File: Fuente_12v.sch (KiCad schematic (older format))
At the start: 3 parts, among them U1 L7812

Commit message: agregado el segundo RDC, leds conectados a +5v, asignados footprints
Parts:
- removed C1: 10µ, symbol Device:CP
- added C1: 10µ, Capacitor_SMD:CP_Elec_4x5.4, symbol Device:CP1
- C2: footprint (none) -> Capacitor_SMD:C_1206_3216Metric_Pad1.42x1.75mm_HandSolder
- U1: footprint (none) -> Package_TO_SOT_THT:TO-218-3_Vertical
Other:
- note added: "Ver la corriente que consumen los RDC \npara no superar 1A que suministra el LM7812"
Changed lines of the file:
@@
 $Descr A4 11693 8268
 encoding utf-8
-Sheet 2 4
+Sheet 5 5
 Title ""
 Date ""
@@
 F 0 "U1" H 3100 2342 50  0000 C CNN
 F 1 "L7812" H 3100 2251 50  0000 C CNN
-F 2 "" H 3125 1950 50  0001 L CIN
+F 2 "Package_TO_SOT_THT:TO-218-3_Vertical" H 3125 1950 50  0001 L CIN
 F 3 "http://www.st.com/content/ccc/resource/technical/document/datasheet/41/4f/b3/b0/12/d4/47/88/CD00000444.pdf/files/CD00000444.pdf/jcr:content/translations/en.CD00000444.pdf" H 3100 2050 50  0001 C CNN
 	1    3100 2100
 	1    0    0    -1
 $EndComp
-$Comp
-L Device:CP C?
-U 1 1 5EF448FC
-P 3600 2250
-AR Path="/5EF448FC" Ref="C?"  Part="1"
-AR Path="/5EF34214/5EF448FC" Ref="C1"  Part="1"
-F 0 "C1" H 3718 2296 50  0000 L CNN
-F 1 "10µ" H 3718 2205 50  0000 L CNN
-F 2 "" H 3638 2100 50  0001 C CNN
-F 3 "~" H 3600 2250 50  0001 C CNN
-	1    3600 2250
-	1    0    0    -1
-$EndComp
-Wire Wire Line
-	3400 2100 3600 2100
 $Comp
 L power:GND #PWR?
@@
 F 0 "C2" H 4165 2296 50  0000 L CNN
 F 1 "0,1µ" H 4165 2205 50  0000 L CNN
-F 2 "" H 4088 2100 50  0001 C CNN
+F 2 "Capacitor_SMD:C_1206_3216Metric_Pad1.42x1.75mm_HandSolder" H 4088 2100 50  0001 C CNN
 F 3 "~" H 4050 2250 50  0001 C CNN
 	1    4050 2250
@@
 Wire Wire Line
 	4050 2400 4050 2450
-Wire Wire Line
-	3600 2100 4050 2100
-Connection ~ 3600 2100
 $Comp
 L power:+12V #PWR?
@@
 Wire Wire Line
 	2500 2100 2800 2100
+$Comp
+L Device:CP1 C1
+U 1 1 5F0A8BCC
+P 3600 2250
+F 0 "C1" H 3715 2296 50  0000 L CNN
+F 1 "10µ" H 3715 2205 50  0000 L CNN
+F 2 "Capacitor_SMD:CP_Elec_4x5.4" H 3600 2250 50  0001 C CNN
+F 3 "~" H 3600 2250 50  0001 C CNN
+	1    3600 2250
+	1    0    0    -1
+$EndComp
+Wire Wire Line
+	3400 2100 3600 2100
+Connection ~ 3600 2100
+Wire Wire Line
+	3600 2100 4050 2100
+Text Notes 2350 1800 0    50   ~ 0
+Ver la corriente que consumen los RDC \npara no superar 1A que suministra el LM7812
 $EndSCHEMATC

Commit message: cambios en el placement
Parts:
- renumbered C1 to C26, C2 to C27, U1 to U3
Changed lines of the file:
@@
 P 3100 2100
 AR Path="/5EF448F6" Ref="U?"  Part="1"
-AR Path="/5EF34214/5EF448F6" Ref="U1"  Part="1"
-F 0 "U1" H 3100 2342 50  0000 C CNN
+AR Path="/5EF34214/5EF448F6" Ref="U3"  Part="1"
+F 0 "U3" H 3100 2342 50  0000 C CNN
 F 1 "L7812" H 3100 2251 50  0000 C CNN
 F 2 "Package_TO_SOT_THT:TO-218-3_Vertical" H 3125 1950 50  0001 L CIN
@@
 P 3100 2450
 AR Path="/5EF44904" Ref="#PWR?"  Part="1"
-AR Path="/5EF34214/5EF44904" Ref="#PWR0102"  Part="1"
-F 0 "#PWR0102" H 3100 2450 30  0001 C CNN
+AR Path="/5EF34214/5EF44904" Ref="#PWR046"  Part="1"
+F 0 "#PWR046" H 3100 2450 30  0001 C CNN
 F 1 "GND" H 3100 2380 30  0001 C CNN
 F 2 "" H 3100 2450 60  0000 C CNN
@@
 P 3600 2450
 AR Path="/5EF4490B" Ref="#PWR?"  Part="1"
-AR Path="/5EF34214/5EF4490B" Ref="#PWR0103"  Part="1"
-F 0 "#PWR0103" H 3600 2450 30  0001 C CNN
+AR Path="/5EF34214/5EF4490B" Ref="#PWR047"  Part="1"
+F 0 "#PWR047" H 3600 2450 30  0001 C CNN
 F 1 "GND" H 3600 2380 30  0001 C CNN
 F 2 "" H 3600 2450 60  0000 C CNN
@@
 P 4050 2250
 AR Path="/5EF44912" Ref="C?"  Part="1"
-AR Path="/5EF34214/5EF44912" Ref="C2"  Part="1"
-F 0 "C2" H 4165 2296 50  0000 L CNN
+AR Path="/5EF34214/5EF44912" Ref="C27"  Part="1"
+F 0 "C27" H 4165 2296 50  0000 L CNN
 F 1 "0,1µ" H 4165 2205 50  0000 L CNN
 F 2 "Capacitor_SMD:C_1206_3216Metric_Pad1.42x1.75mm_HandSolder" H 4088 2100 50  0001 C CNN
@@
 P 4050 2450
 AR Path="/5EF44918" Ref="#PWR?"  Part="1"
-AR Path="/5EF34214/5EF44918" Ref="#PWR0104"  Part="1"
-F 0 "#PWR0104" H 4050 2450 30  0001 C CNN
+AR Path="/5EF34214/5EF44918" Ref="#PWR048"  Part="1"
+F 0 "#PWR048" H 4050 2450 30  0001 C CNN
 F 1 "GND" H 4050 2380 30  0001 C CNN
 F 2 "" H 4050 2450 60  0000 C CNN
@@
 P 4500 2100
 AR Path="/5EF44921" Ref="#PWR?"  Part="1"
-AR Path="/5EF34214/5EF44921" Ref="#PWR0105"  Part="1"
-F 0 "#PWR0105" H 4500 1950 50  0001 C CNN
+AR Path="/5EF34214/5EF44921" Ref="#PWR045"  Part="1"
+F 0 "#PWR045" H 4500 1950 50  0001 C CNN
 F 1 "+12V" H 4515 2273 50  0000 C CNN
 F 2 "" H 4500 2100 50  0001 C CNN
@@
 P 2500 2100
 AR Path="/5EF448F0" Ref="#PWR?"  Part="1"
-AR Path="/5EF34214/5EF448F0" Ref="#PWR0101"  Part="1"
-F 0 "#PWR0101" H 2500 1950 50  0001 C CNN
+AR Path="/5EF34214/5EF448F0" Ref="#PWR044"  Part="1"
+F 0 "#PWR044" H 2500 1950 50  0001 C CNN
 F 1 "+24V" H 2515 2273 50  0000 C CNN
 F 2 "" H 2500 2100 50  0001 C CNN
@@
 	2500 2100 2800 2100
 $Comp
-L Device:CP1 C1
+L Device:CP1 C26
 U 1 1 5F0A8BCC
 P 3600 2250
-F 0 "C1" H 3715 2296 50  0000 L CNN
+F 0 "C26" H 3715 2296 50  0000 L CNN
 F 1 "10µ" H 3715 2205 50  0000 L CNN
 F 2 "Capacitor_SMD:CP_Elec_4x5.4" H 3600 2250 50  0001 C CNN

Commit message: reubicados componentes, cambiado regulador a SMD
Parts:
- U3: footprint Package_TO_SOT_THT:TO-218-3_Vertical -> Package_TO_SOT_SMD:TO-252-3_TabPin2
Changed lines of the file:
@@
 F 0 "U3" H 3100 2342 50  0000 C CNN
 F 1 "L7812" H 3100 2251 50  0000 C CNN
-F 2 "Package_TO_SOT_THT:TO-218-3_Vertical" H 3125 1950 50  0001 L CIN
+F 2 "Package_TO_SOT_SMD:TO-252-3_TabPin2" H 3125 1950 50  0001 L CIN
 F 3 "http://www.st.com/content/ccc/resource/technical/document/datasheet/41/4f/b3/b0/12/d4/47/88/CD00000444.pdf/files/CD00000444.pdf/jcr:content/translations/en.CD00000444.pdf" H 3100 2050 50  0001 C CNN
 	1    3100 2100

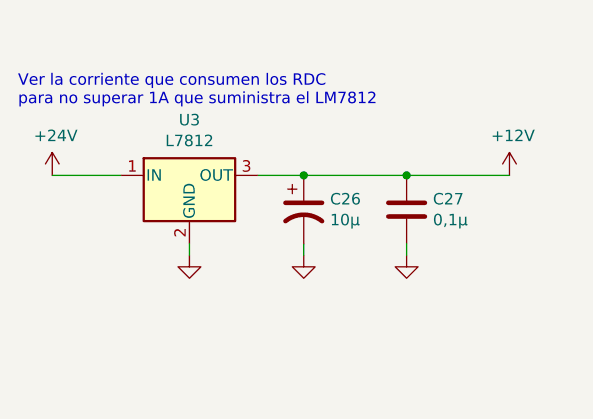
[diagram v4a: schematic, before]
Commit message: cambiado a conectores MOLEX KK, agregados test points para señales analogicas
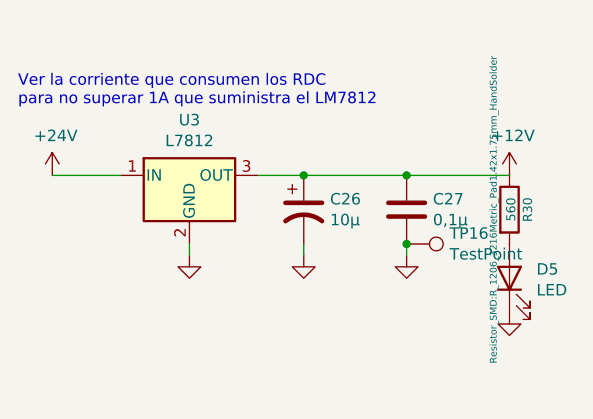
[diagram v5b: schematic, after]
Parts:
- added D5: LED, LED_SMD:LED_1206_3216Metric_Pad1.42x1.75mm_HandSolder, symbol Device:LED
- added R30: 560, Resistor_SMD:R_1206_3216Metric_Pad1.42x1.75mm_HandSolder, symbol Device:R
- added TP16: TestPoint, TestPoint:TestPoint_THTPad_1.0x1.0mm_Drill0.5mm, symbol Connector:TestPoint
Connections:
- net +12V: now also R30.1
- net GND: now also D5.1 (K), TP16.1
- new net: D5.2 (A), R30.2
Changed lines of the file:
@@
 Text Notes 2350 1800 0    50   ~ 0
 Ver la corriente que consumen los RDC \npara no superar 1A que suministra el LM7812
+$Comp
+L Device:R R?
+U 1 1 5F0B9D9B
+P 4500 2250
+AR Path="/5F0B9D9B" Ref="R?"  Part="1"
+AR Path="/5EF45E27/5F0B9D9B" Ref="R?"  Part="1"
+AR Path="/5F077C82/5F0B9D9B" Ref="R?"  Part="1"
+AR Path="/5EF34214/5F0B9D9B" Ref="R30"  Part="1"
+F 0 "R30" V 4580 2250 40  0000 C CNN
+F 1 "560" V 4507 2251 40  0000 C CNN
+F 2 "Resistor_SMD:R_1206_3216Metric_Pad1.42x1.75mm_HandSolder" V 4430 2250 30  0000 C CNN
+F 3 "~" H 4500 2250 30  0000 C CNN
+	1    4500 2250
+	1    0    0    -1
+$EndComp
+$Comp
+L Device:LED D?
+U 1 1 5F0B9DA1
+P 4500 2550
+AR Path="/5F0B9DA1" Ref="D?"  Part="1"
+AR Path="/5EF45E27/5F0B9DA1" Ref="D?"  Part="1"
+AR Path="/5F077C82/5F0B9DA1" Ref="D?"  Part="1"
+AR Path="/5EF34214/5F0B9DA1" Ref="D5"  Part="1"
+F 0 "D5" V 4539 2432 50  0000 R CNN
+F 1 "LED" V 4448 2432 50  0000 R CNN
+F 2 "LED_SMD:LED_1206_3216Metric_Pad1.42x1.75mm_HandSolder" H 4500 2550 50  0001 C CNN
+F 3 "~" H 4500 2550 50  0001 C CNN
+	1    4500 2550
+	0    -1   -1   0
+$EndComp
+$Comp
+L power:GND #PWR?
+U 1 1 5F0B9E47
+P 4500 2700
+AR Path="/5F0B9E47" Ref="#PWR?"  Part="1"
+AR Path="/5EF34214/5F0B9E47" Ref="#PWR057"  Part="1"
+F 0 "#PWR057" H 4500 2700 30  0001 C CNN
+F 1 "GND" H 4500 2630 30  0001 C CNN
+F 2 "" H 4500 2700 60  0000 C CNN
+F 3 "" H 4500 2700 60  0000 C CNN
+	1    4500 2700
+	1    0    0    -1
+$EndComp
+$Comp
+L Connector:TestPoint TP16
+U 1 1 5F0BA374
+P 4050 2400
+F 0 "TP16" V 4004 2588 50  0000 L CNN
+F 1 "TestPoint" V 4095 2588 50  0000 L CNN
+F 2 "TestPoint:TestPoint_THTPad_1.0x1.0mm_Drill0.5mm" H 4250 2400 50  0001 C CNN
+F 3 "~" H 4250 2400 50  0001 C CNN
+	1    4050 2400
+	0    1    1    0
+$EndComp
+Connection ~ 4050 2400
 $EndSCHEMATC

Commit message: outline reducido, para revision por peers
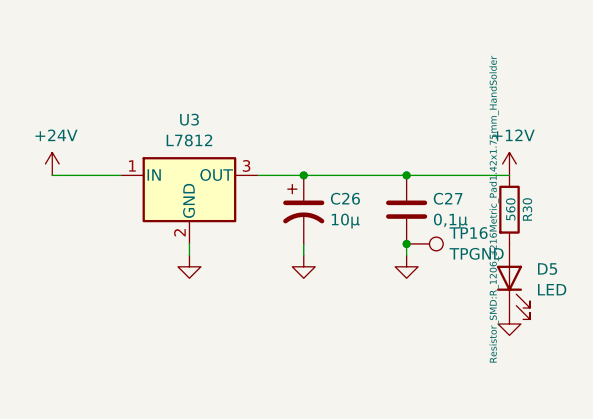
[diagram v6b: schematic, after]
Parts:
- TP16: value TestPoint -> TPGND
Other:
- note removed: "Ver la corriente que consumen los RDC \npara no superar 1A que suministra el LM7812"
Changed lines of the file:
@@
 Wire Wire Line
 	3600 2100 4050 2100
-Text Notes 2350 1800 0    50   ~ 0
-Ver la corriente que consumen los RDC \npara no superar 1A que suministra el LM7812
 $Comp
 L Device:R R?
@@
 P 4050 2400
 F 0 "TP16" V 4004 2588 50  0000 L CNN
-F 1 "TestPoint" V 4095 2588 50  0000 L CNN
+F 1 "TPGND" V 4095 2588 50  0000 L CNN
 F 2 "TestPoint:TestPoint_THTPad_1.0x1.0mm_Drill0.5mm" H 4250 2400 50  0001 C CNN
 F 3 "~" H 4250 2400 50  0001 C CNN
